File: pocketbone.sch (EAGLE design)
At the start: 61 parts, among them J1 USD_CONNECTOR, U5 24LC_32AT-I/OT, U6 SN74LVC1G07_DCK_5, Y1 CM200C-32.768KAZF-UT, Y2 445C33D24M00000

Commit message: Consolidate library
* Renumber parts
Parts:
- removed R135: 100K,1%, Strawson_Eagle_Lib:RESISTOR0402-RES
- removed R61, R62, R63, R64: 240, Strawson_Eagle_Lib:RESISTOR0402-RES
- removed SIP: OSD3358, BeagleBone_Blue:OSD3358
- removed U5: 24LC_32AT-I/OT, Microchip-24LCxxx:24LC_32AT-I/OT
- removed U6: SN74LVC1G07_DCK_5, BeagleBone_Blue:SN74LVC1G07_DCK_5
- removed USB0, USB1: USB-MICRO-SMD, Strawson_Eagle_Lib:USB-AB
- added JP1, JP2: USB-MICRO-SMD, pocketbone:USB-AB
- added R27, R28: 100K,1%, Strawson_Eagle_Lib:RESISTOR0402-RES
- added R5, R6: 1.5K,1%, Strawson_Eagle_Lib:RESISTOR0402-RES
- added R9: 4.87k, Strawson_Eagle_Lib:RESISTOR0402-RES
- added U1: 24LC_32AT-I/OT, pocketbone:24LC_32AT-I/OT
- added U2: OSD3358, pocketbone:OSD3358
- added U3: SN74LVC1G07_DCK_5, pocketbone:SN74LVC1G07_DCK_5
- J1: device BeagleBone_Blue:USD_CONNECTOR -> pocketbone:USD_CONNECTOR
- R1, R3, R4: value 100K,1% -> 240
- R2: value 1.5K,1% -> 240
- R23: value 1.5K,1% -> 100K,1%
- R24: value 4.87k -> 100K,1%
- Y1: value CM200C-32.768KAZF-UT -> 445C33D24M00000; device CM200C-32.768KAZF-UT:CM200C-32.768KAZF-UT -> pocketbone:445C33D24M00000
- Y2: value 445C33D24M00000 -> CM200C-32.768KAZF-UT; device 445C33D24M00000:445C33D24M00000 -> pocketbone:CM200C-32.768KAZF-UT
- renumbered C27 to C8, C28 to C1, C29 to C5, C30 to C7, C31 to C6, C32 to C4, C33 to C9, C34 to C2, C35 to C3, C45 to C11, C46 to C10, D10 to D1, D11 to D2, D12 to D3, D13 to D4, D8 to D5, L4 to L2, L5 to L1, POWER to S1, R113 to R13, R115 to R14, R116 to R15, R118 to R16, R120 to R17, R122 to R18, R125 to R19, R127 to R20, R129 to R21, R131 to R22, R140 to R25, R143 to R26, R152 to R11, R153 to R12, R158 to R29, R58 to R7, R59 to R8, R60 to R10, RESET to S2
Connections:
- net 3.3V: now also R5.2, R6.2, U1.VCC, U2A.VOUT_USER_3P3V_0, U2A.VOUT_USER_3P3V_1; no longer R2.2, R23.2, SIPA.VOUT_USER_3P3V_0, SIPA.VOUT_USER_3P3V_1, U5.VCC
- net 5.0V: now also U2A.VIN_AC_0, U2A.VIN_AC_1; no longer SIPA.VIN_AC_0, SIPA.VIN_AC_1
- net BATT_LED_2: now also U2C.LCD_DATA15_T5; no longer SIPC.LCD_DATA15_T5
- net EQEP_1A: now also R27.2, U2C.LCD_DATA12_V2; no longer R1.2, SIPC.LCD_DATA12_V2
- net EQEP_1B: now also R28.2, U2C.LCD_DATA13_V3; no longer R3.2, SIPC.LCD_DATA13_V3
- net GND: now also JP2.GND, JP2.SHIELD, R2.1, R23.1, R24.1, R27.1, R28.1, R9.2, U1.VSS, U2F.DGND1, U2F.DGND19, U2F.DGND36, U2F.DGND42, U2F.DGND45, U2F.DGND46, U2F.DGND59, U2F.DGND61, U2F.DGND62, U2F.DGND71, U2F.DGND80, U2F.DGND86, U3.GND; no longer R135.1, R24.2, R61.1, R62.1, R63.1, R64.1, SIPF.DGND1, SIPF.DGND19, SIPF.DGND36, SIPF.DGND42, SIPF.DGND45, SIPF.DGND46, SIPF.DGND59, SIPF.DGND61, SIPF.DGND62, SIPF.DGND71, SIPF.DGND80, SIPF.DGND86, U5.VSS, U6.GND, USB0.GND, USB0.SHIELD
- net I2C0_SCL: now also R6.1, U1.SCL, U2A.I2C0_SCL, U2A.PMIC_I2C_SCL; no longer R23.1, SIPA.I2C0_SCL, SIPA.PMIC_I2C_SCL, U5.SCL
- net I2C0_SDA: now also R5.1, U1.SDA, U2A.I2C0_SDA, U2A.PMIC_I2C_SDA; no longer R2.1, SIPA.I2C0_SDA, SIPA.PMIC_I2C_SDA, U5.SDA
- net LCD_DATA_14: now also U2C.LCD_DATA14_V4; no longer SIPC.LCD_DATA14_V4
- net LDO_PGOOD: now also U2A.PMIC_OUT_LDO_PGOOD, U2B.RTC_PWRONRSTN; no longer SIPA.PMIC_OUT_LDO_PGOOD, SIPB.RTC_PWRONRSTN
- net MDIR_2B: now also R24.2, U2C.LCD_DATA11_U4; no longer R135.2, SIPC.LCD_DATA11_U4
- net MDIR_3A: now also U2C.LCD_DATA3_R4; no longer SIPC.LCD_DATA3_R4
- net MDIR_3B: now also U2C.LCD_DATA2_R3; no longer SIPC.LCD_DATA2_R3
- net MDIR_4A: now also U2C.LCD_DATA0_R1; no longer SIPC.LCD_DATA0_R1
- net MDIR_4B: now also U2C.LCD_DATA1_R2; no longer SIPC.LCD_DATA1_R2
- net N$1: now also JP1.VBUS; no longer USB1.VBUS
- net N$12: now also U2A.PMIC_IN_PWR_EN, U2A.PMIC_POWER_EN; no longer SIPA.PMIC_IN_PWR_EN, SIPA.PMIC_POWER_EN
- net N$128: now also JP1.GND, JP1.SHIELD; no longer USB1.GND, USB1.SHIELD
- net N$129: now also U2C.USB1_VBUS; no longer SIPC.USB1_VBUS
- net N$131: now also U2E.RTC_KALDO_ENN; no longer SIPE.RTC_KALDO_ENN
- net N$2: now also U2B.MMC0_CLK_G17; no longer SIPB.MMC0_CLK_G17
- net N$26: now also U2B.OSC0_IN, Y2.2; no longer SIPB.OSC0_IN, Y1.2
- net N$27: now also U2B.OSC0_OUT, Y2.1; no longer SIPB.OSC0_OUT, Y1.1
- net N$28: now also U1.WP; no longer U5.WP
- net N$31: now also U2B.OSC0_GND; no longer SIPB.OSC0_GND
- net N$32: now also U2B.OSC1_IN, Y1.2; no longer SIPB.OSC1_IN, Y2.2
- net N$33: now also U2B.OSC1_OUT, Y1.1; no longer SIPB.OSC1_OUT, Y2.1
- net N$34: now also U2B.OSC1_GND; no longer SIPB.OSC1_GND
- net N$42: now also U2B.JTAG_TRSTN; no longer SIPB.JTAG_TRSTN
- net N$43: now also U2B.USR3_V16; no longer SIPB.USR3_V16
- net N$44: now also U2B.USR2_T15; no longer SIPB.USR2_T15
- net N$45: now also U2B.USR1_U15; no longer SIPB.USR1_U15
- net N$46: now also U2B.USR0_V15; no longer SIPB.USR0_V15
- net N$47: now also R1.2; no longer R61.2
- net N$5: now also U2B.MMC0_DAT3_F17; no longer SIPB.MMC0_DAT3_F17
- net N$57: now also R2.2; no longer R62.2
- net N$58: now also R3.2; no longer R63.2
- net N$59: now also R4.2; no longer R64.2
- net N$70: now also U2B.MMC0_DAT1_G15; no longer SIPB.MMC0_DAT1_G15
- net N$74: now also U2B.MMC0_CMD_G18; no longer SIPB.MMC0_CMD_G18
- net N$75: now also U2B.MMC0_CD_C15; no longer SIPB.MMC0_CD_C15
- net N$77: now also U2B.MMC0_DAT0_G16; no longer SIPB.MMC0_DAT0_G16
- net NTE: now also U2B.MMC0_DAT2_F18; no longer SIPB.MMC0_DAT2_F18
- net PMIC_INT: now also U2A.PMIC_OUT_NINT, U2B.EXTINTN; no longer SIPA.PMIC_OUT_NINT, SIPB.EXTINTN
- net PMIC_NWAKEUP: now also U2A.PMIC_OUT_NWAKEUP, U2B.EXT_WAKEUP; no longer SIPA.PMIC_OUT_NWAKEUP, SIPB.EXT_WAKEUP
- net PMIC_PGOOD: now also U2A.PMIC_OUT_PGOOD, U2B.PWRONRSTN, U3.A; no longer SIPA.PMIC_OUT_PGOOD, SIPB.PWRONRSTN, U6.A
- net PWR: now also U2A.PMIC_IN_PB_IN; no longer SIPA.PMIC_IN_PB_IN
- net PWR_LEDR: now also R9.1; no longer R24.1
- net RESET: now also U2B.WARMRSTN, U3.Y; no longer SIPB.WARMRSTN, U6.Y
- net SERVO_EN: now also R23.2, U2C.LCD_DATA10_U3; no longer R4.2, SIPC.LCD_DATA10_U3
- net SVO5: now also U2C.LCD_DATA6_T3; no longer SIPC.LCD_DATA6_T3
- net SVO6: now also U2C.LCD_DATA7_T4; no longer SIPC.LCD_DATA7_T4
- net SVO7: now also U2C.LCD_DATA4_T1; no longer SIPC.LCD_DATA4_T1
- net SVO8: now also U2C.LCD_DATA5_T2; no longer SIPC.LCD_DATA5_T2
- net SYS_5V: now also U2A.VOUT_SYS_5V_0, U2A.VOUT_SYS_5V_1; no longer SIPA.VOUT_SYS_5V_0, SIPA.VOUT_SYS_5V_1
- net UART5_RX: now also U2C.LCD_DATA9_U2; no longer SIPC.LCD_DATA9_U2
- net UART5_TX: now also U2C.LCD_DATA8_U1; no longer SIPC.LCD_DATA8_U1
- net USB0_DM: now also JP2.D-, U2C.USB0_DM; no longer SIPC.USB0_DM, USB0.D-
- net USB0_DP: now also JP2.D+, U2C.USB0_DP; no longer SIPC.USB0_DP, USB0.D+
- net USB0_ID: now also JP2.USBID, U2C.USB0_ID; no longer SIPC.USB0_ID, USB0.USBID
- net USB1_DM: now also JP1.D-, U2C.USB1_DM; no longer SIPC.USB1_DM, USB1.D-
- net USB1_DP: now also JP1.D+, U2C.USB1_DP; no longer SIPC.USB1_DP, USB1.D+
- net USB1_ID: now also JP1.USBID, U2C.USB1_ID; no longer SIPC.USB1_ID, USB1.USBID
- net USB_DC: now also JP2.VBUS, U2A.VIN_USB_0, U2A.VIN_USB_1, U2C.USB0_VBUS; no longer SIPA.VIN_USB_0, SIPA.VIN_USB_1, SIPC.USB0_VBUS, USB0.VBUS
- net VDD_1V8: now also U2A.VOUT_LDO3_1P8V_0, U2A.VOUT_LDO3_1P8V_1, U2E.VDD_1V83, U2E.VDD_1V84; no longer SIPA.VOUT_LDO3_1P8V_0, SIPA.VOUT_LDO3_1P8V_1, SIPE.VDD_1V83, SIPE.VDD_1V84
- net VDD_3V3AUX: now also U2A.VOUT_LDO2_3P3V; no longer SIPA.VOUT_LDO2_3P3V
- net VDD_RTC: now also U2E.VDD_RTC3, U3.VCC; no longer SIPE.VDD_RTC3, U6.VCC

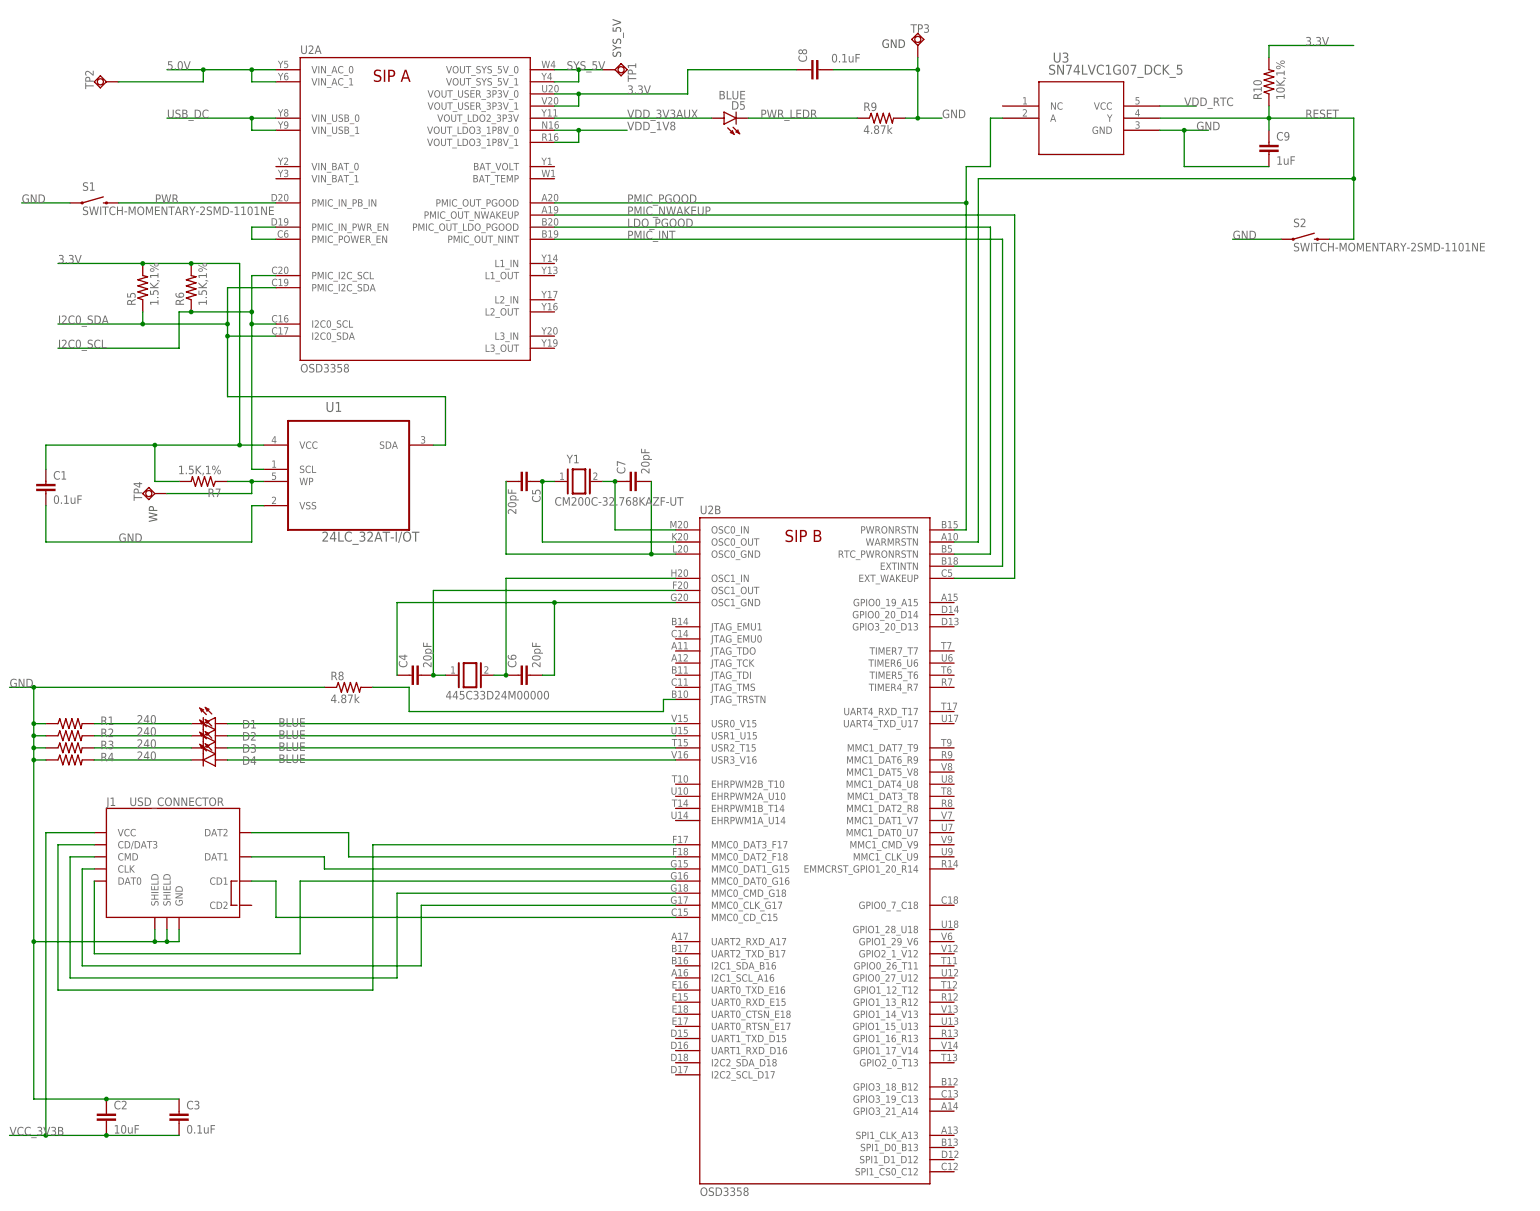
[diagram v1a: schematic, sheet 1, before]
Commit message: Update some ref designators
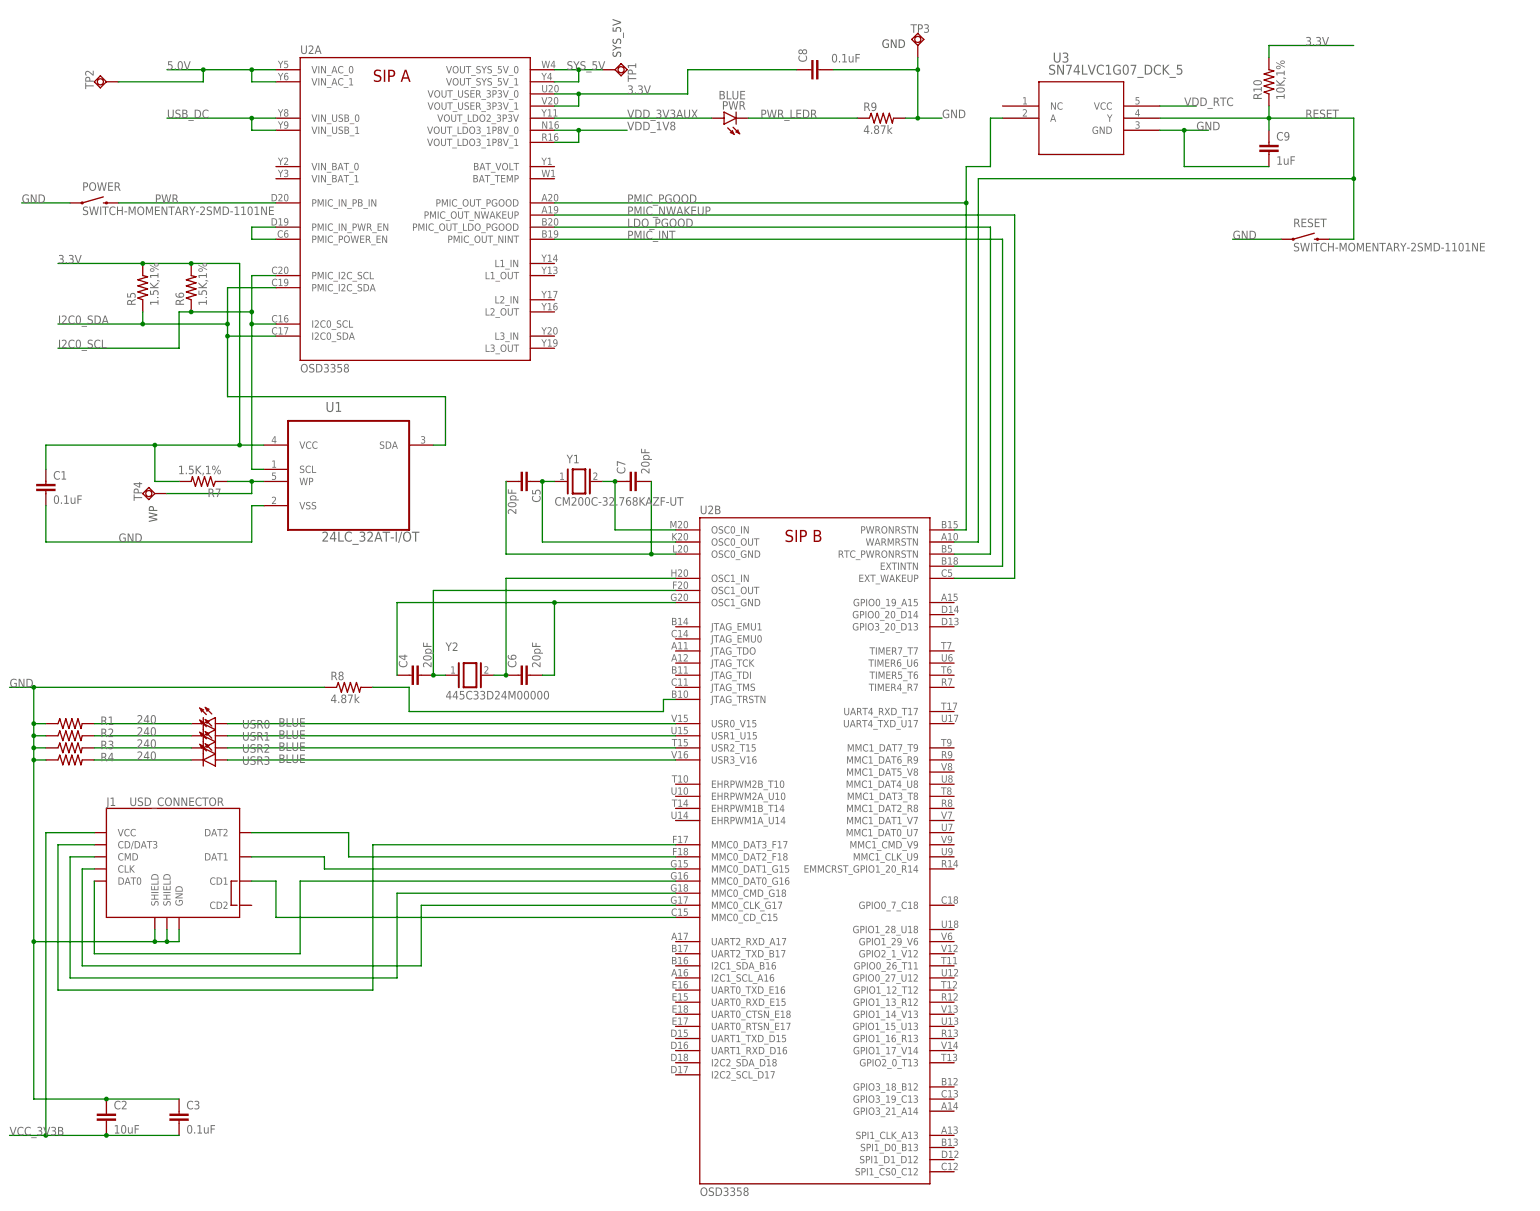
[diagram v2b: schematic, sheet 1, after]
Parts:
- Y1: value 445C33D24M00000 -> CM200C-32.768KAZF-UT; device pocketbone:445C33D24M00000 -> pocketbone:CM200C-32.768KAZF-UT
- Y2: value CM200C-32.768KAZF-UT -> 445C33D24M00000; device pocketbone:CM200C-32.768KAZF-UT -> pocketbone:445C33D24M00000
- renumbered D1 to USR0, D2 to USR1, D3 to USR2, D4 to USR3, D5 to PWR, S1 to POWER, S2 to RESET
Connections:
- net N$26: now also Y1.2; no longer Y2.2
- net N$27: now also Y1.1; no longer Y2.1
- net N$32: now also Y2.2; no longer Y1.2
- net N$33: now also Y2.1; no longer Y1.1

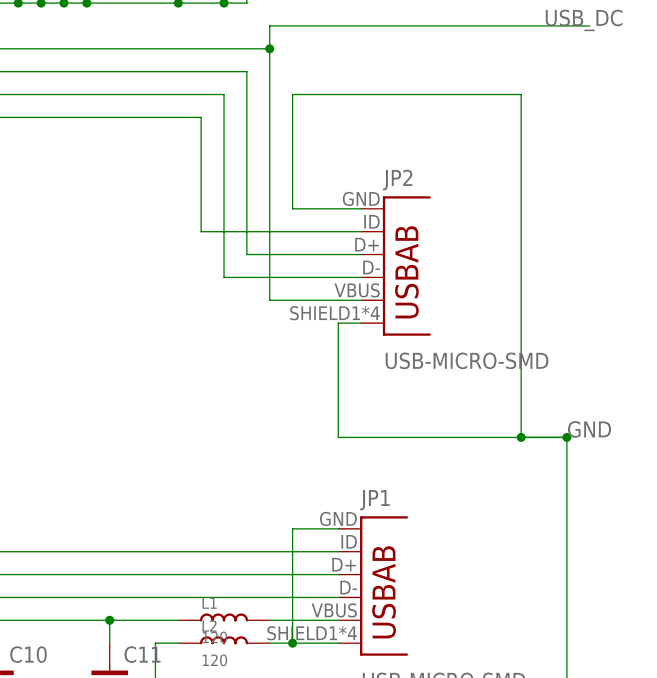
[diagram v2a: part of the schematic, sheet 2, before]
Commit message: Rename USB connectors
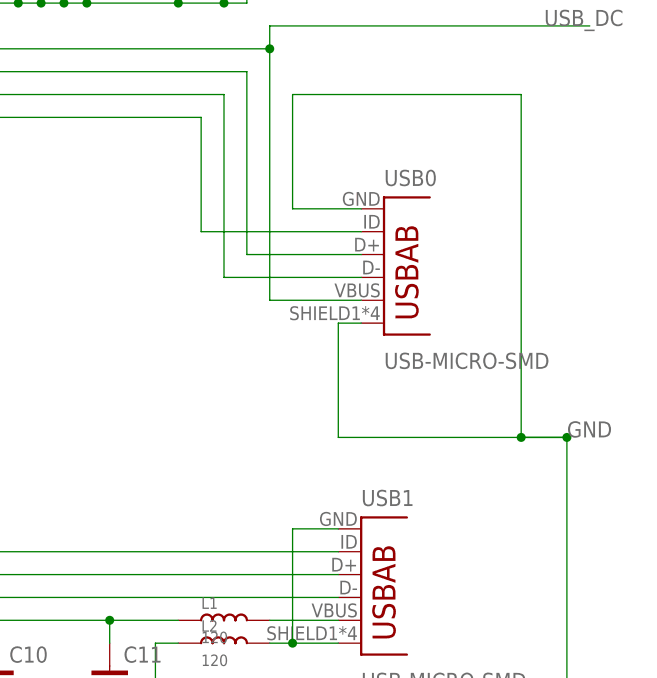
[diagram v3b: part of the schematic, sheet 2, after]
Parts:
- renumbered JP1 to USB1, JP2 to USB0
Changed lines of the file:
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@@
 <part name="U3" library="pocketbone" deviceset="SN74LVC1G07_DCK_5" device=""/>
 <part name="R29" library="Strawson_Eagle_Lib" deviceset="RESISTOR" device="0402-RES" value="10K,1%"/>
-<part name="JP2" library="pocketbone" deviceset="USB-AB" device="" value="USB-MICRO-SMD"/>
+<part name="USB0" library="pocketbone" deviceset="USB-AB" device="" value="USB-MICRO-SMD"/>
 <part name="J1" library="pocketbone" deviceset="USD_CONNECTOR" device=""/>
-<part name="JP1" library="pocketbone" deviceset="USB-AB" device="" value="USB-MICRO-SMD"/>
+<part name="USB1" library="pocketbone" deviceset="USB-AB" device="" value="USB-MICRO-SMD"/>
 <part name="TP2" library="testpad" deviceset="TPSQ" device="B1,27">
 <attribute name="TP_SIGNAL_NAME" value="5.0V"/>
@@
 </instance>
 <instance part="FRAME2" gate="G$1" x="0" y="0"/>
-<instance part="JP2" gate="G$1" x="325.12" y="104.14"/>
-<instance part="JP1" gate="G$1" x="322.58" y="68.58"/>
+<instance part="USB0" gate="G$1" x="325.12" y="104.14"/>
+<instance part="USB1" gate="G$1" x="322.58" y="68.58"/>
 <instance part="R27" gate="G$1" x="304.8" y="142.24" smashed="yes" rot="R90">
 <attribute name="NAME" x="303.3014" y="138.43" size="1.27" layer="95" rot="R90" align="center-right"/>
@@
 <junction x="292.1" y="53.34"/>
 <pinref part="C10" gate="G$1" pin="2"/>
-<pinref part="JP2" gate="G$1" pin="GND"/>
+<pinref part="USB0" gate="G$1" pin="GND"/>
 <wire x1="320.04" y1="109.22" x2="312.42" y2="109.22" width="0.1524" layer="91"/>
-<pinref part="JP2" gate="G$1" pin="SHIELD"/>
+<pinref part="USB0" gate="G$1" pin="SHIELD"/>
 <wire x1="320.04" y1="96.52" x2="317.5" y2="96.52" width="0.1524" layer="91"/>
 <wire x1="317.5" y1="96.52" x2="317.5" y2="83.82" width="0.1524" layer="91"/>
@@
 <label x="195.58" y="139.7" size="1.778" layer="95"/>
 <wire x1="307.34" y1="124.46" x2="307.34" y2="104.14" width="0.1524" layer="91"/>
-<pinref part="JP2" gate="G$1" pin="D+"/>
+<pinref part="USB0" gate="G$1" pin="D+"/>
 <wire x1="307.34" y1="104.14" x2="320.04" y2="104.14" width="0.1524" layer="91"/>
 </segment>
@@
 <label x="195.58" y="137.16" size="1.778" layer="95"/>
 <wire x1="304.8" y1="121.92" x2="304.8" y2="101.6" width="0.1524" layer="91"/>
-<pinref part="JP2" gate="G$1" pin="D-"/>
+<pinref part="USB0" gate="G$1" pin="D-"/>
 <wire x1="304.8" y1="101.6" x2="320.04" y2="101.6" width="0.1524" layer="91"/>
 </segment>
@@
 <wire x1="302.26" y1="119.38" x2="302.26" y2="106.68" width="0.1524" layer="91"/>
 <wire x1="302.26" y1="106.68" x2="320.04" y2="106.68" width="0.1524" layer="91"/>
-<pinref part="JP2" gate="G$1" pin="USBID"/>
+<pinref part="USB0" gate="G$1" pin="USBID"/>
 <label x="195.58" y="132.08" size="1.778" layer="95"/>
 </segment>
@@
 <wire x1="274.32" y1="88.9" x2="274.32" y2="68.58" width="0.1524" layer="91"/>
 <label x="195.58" y="121.92" size="1.778" layer="95"/>
-<pinref part="JP1" gate="G$1" pin="D+"/>
+<pinref part="USB1" gate="G$1" pin="D+"/>
 <wire x1="274.32" y1="68.58" x2="317.5" y2="68.58" width="0.1524" layer="91"/>
 </segment>
@@
 <wire x1="266.7" y1="86.36" x2="266.7" y2="66.04" width="0.1524" layer="91"/>
 <label x="195.58" y="119.38" size="1.778" layer="95"/>
-<pinref part="JP1" gate="G$1" pin="D-"/>
+<pinref part="USB1" gate="G$1" pin="D-"/>
 <wire x1="266.7" y1="66.04" x2="317.5" y2="66.04" width="0.1524" layer="91"/>
 </segment>
@@
 <segment>
 <pinref part="L2" gate="L" pin="2"/>
-<pinref part="JP1" gate="G$1" pin="SHIELD"/>
+<pinref part="USB1" gate="G$1" pin="SHIELD"/>
 <wire x1="309.88" y1="60.96" x2="312.42" y2="60.96" width="0.1524" layer="91"/>
-<pinref part="JP1" gate="G$1" pin="GND"/>
+<pinref part="USB1" gate="G$1" pin="GND"/>
 <wire x1="312.42" y1="60.96" x2="317.5" y2="60.96" width="0.1524" layer="91"/>
 <wire x1="317.5" y1="73.66" x2="312.42" y2="73.66" width="0.1524" layer="91"/>
@@
 <wire x1="190.5" y1="127" x2="309.88" y2="127" width="0.1524" layer="91"/>
 <junction x="309.88" y="127"/>
-<pinref part="JP2" gate="G$1" pin="VBUS"/>
+<pinref part="USB0" gate="G$1" pin="VBUS"/>
 <wire x1="309.88" y1="99.06" x2="320.04" y2="99.06" width="0.1524" layer="91"/>
 <pinref part="U2" gate="C" pin="USB0_VBUS"/>
@@
 <wire x1="190.5" y1="114.3" x2="276.86" y2="114.3" width="0.1524" layer="91"/>
 <wire x1="276.86" y1="114.3" x2="276.86" y2="71.12" width="0.1524" layer="91"/>
-<pinref part="JP1" gate="G$1" pin="USBID"/>
+<pinref part="USB1" gate="G$1" pin="USBID"/>
 <wire x1="276.86" y1="71.12" x2="317.5" y2="71.12" width="0.1524" layer="91"/>
 <label x="195.58" y="114.3" size="1.778" layer="95"/>
@@
 <segment>
 <pinref part="L1" gate="L" pin="2"/>
-<pinref part="JP1" gate="G$1" pin="VBUS"/>
+<pinref part="USB1" gate="G$1" pin="VBUS"/>
 <wire x1="309.88" y1="63.5" x2="317.5" y2="63.5" width="0.1524" layer="91"/>
 </segment>
